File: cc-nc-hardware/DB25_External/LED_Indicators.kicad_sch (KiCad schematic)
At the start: 6 parts, among them U8 74HC14

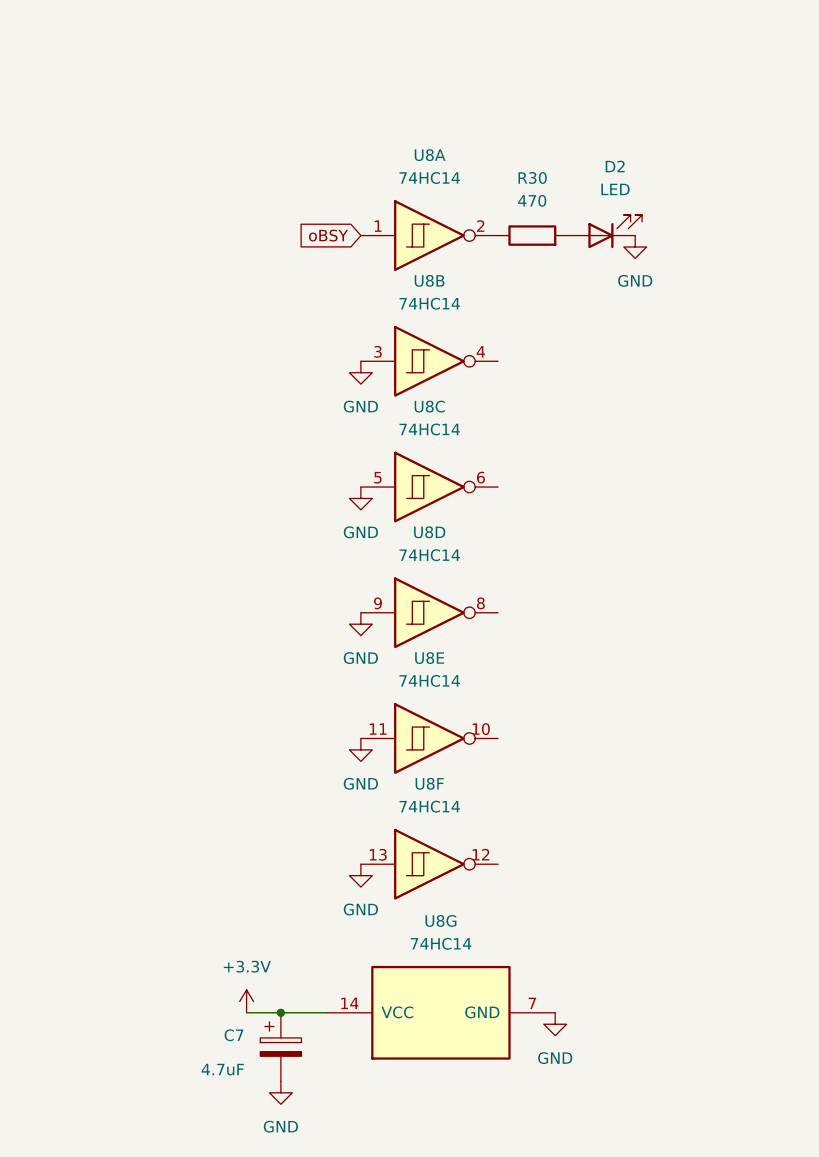
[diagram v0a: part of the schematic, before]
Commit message: DB25 2023_06a, Smaller Design
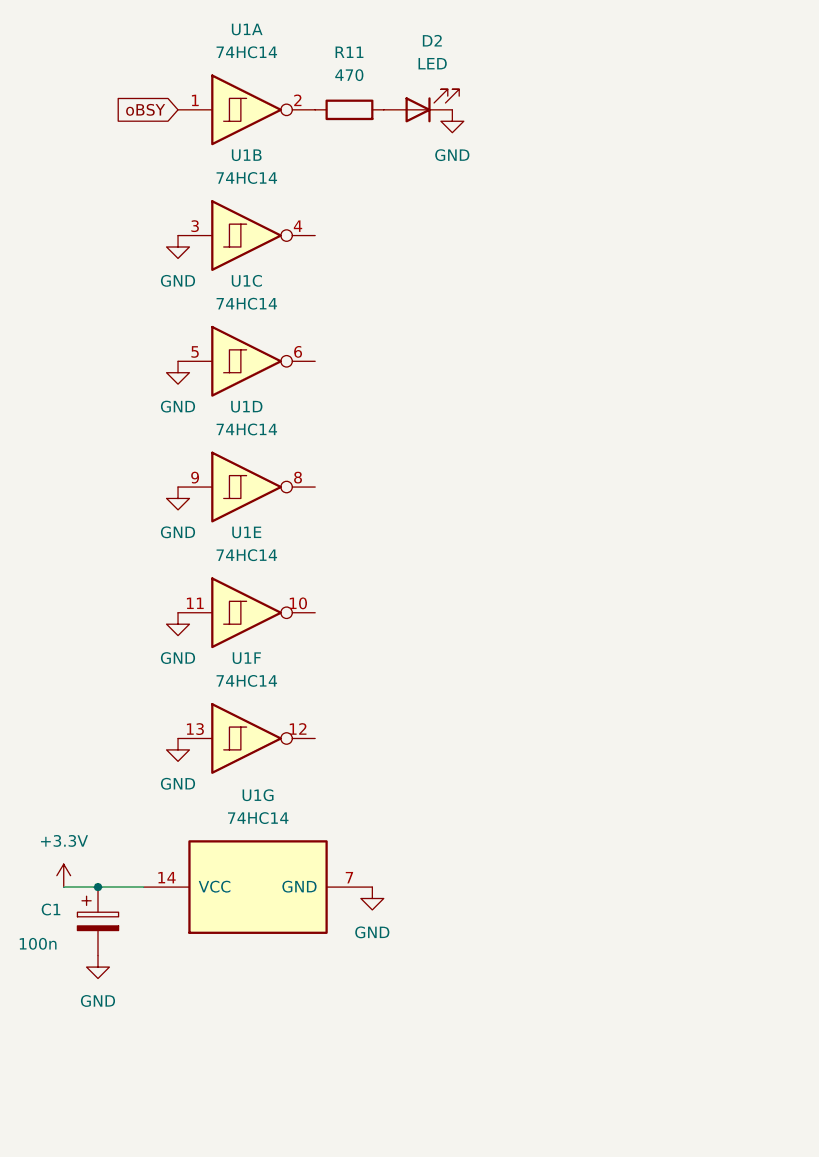
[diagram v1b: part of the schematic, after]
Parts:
- removed C7: 4.7uF, Capacitor_SMD:C_0805_2012Metric_Pad1.18x1.45mm_HandSolder, symbol Device:CP
- removed R30: 470, Resistor_SMD:R_0402_1005Metric_Pad0.72x0.64mm_HandSolder, symbol Device:R
- removed U8: 74HC14, symbol 74xx:74HC14
- added C1: 100n, Capacitor_SMD:C_0805_2012Metric_Pad1.18x1.45mm_HandSolder, symbol Device:CP
- added R11: 470, Resistor_SMD:R_0603_1608Metric_Pad0.98x0.95mm_HandSolder, symbol Device:R
- added U1: 74HC14, symbol 74xx:74HC14
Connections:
- net +3V3: now also C1.1, U1.14 (VCC)
- net GND: now also C1.2, U1.11, U1.13, U1.3, U1.5, U1.7 (GND), U1.9
- net oBSY: now also U1.1
- net at D2.2 (A): now also R11.2
- new net: R11.1, U1.2

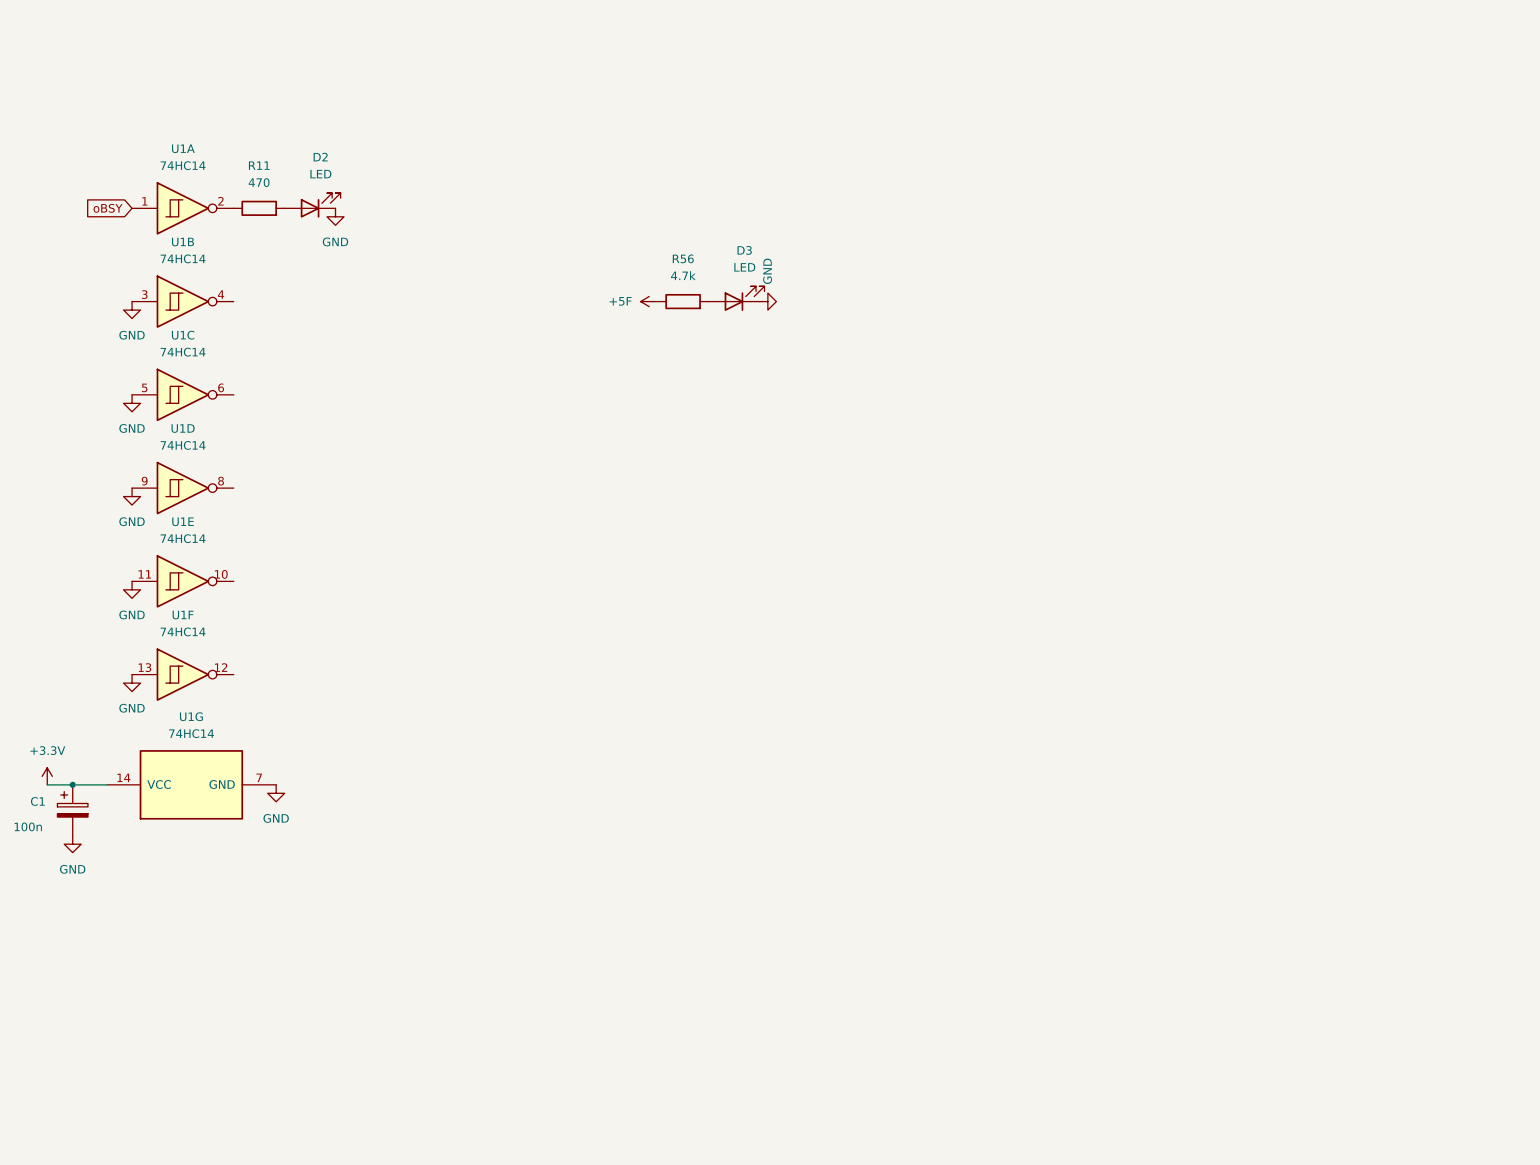
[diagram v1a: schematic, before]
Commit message: Update DB25 schematic for greater clarity
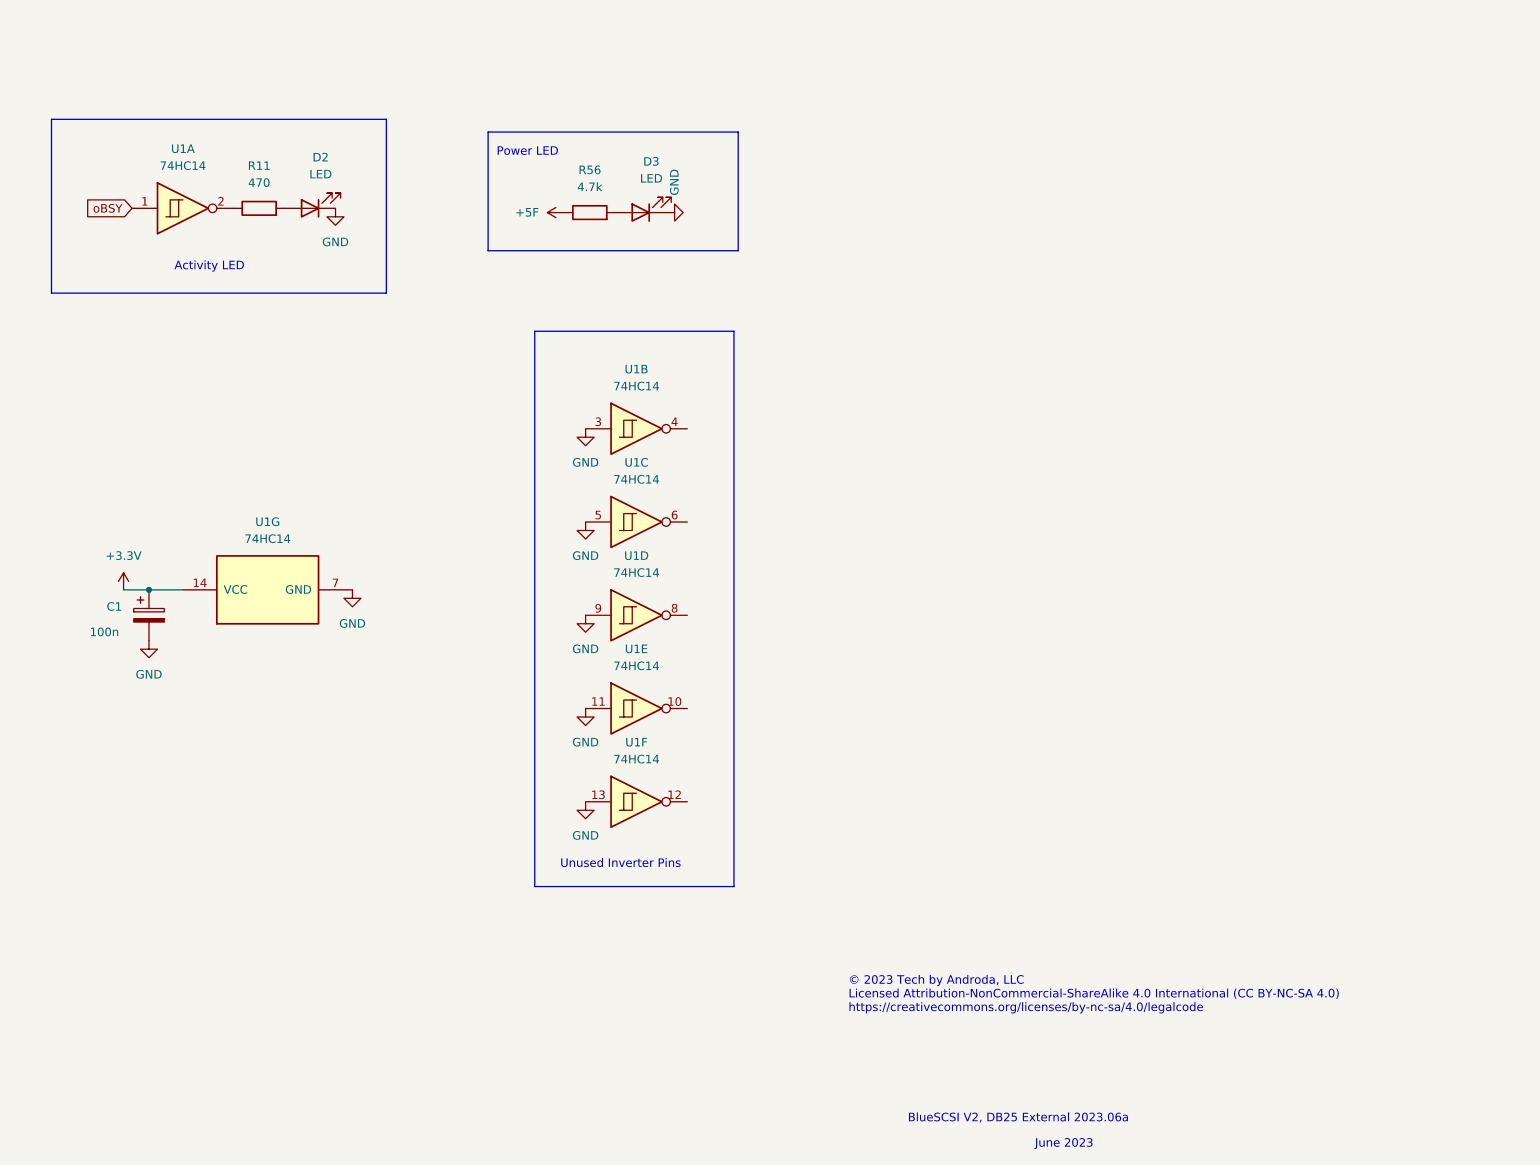
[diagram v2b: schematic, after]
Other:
- note added: "Activity LED"
- note added: "BlueSCSI V2, DB25 External 2023.06a"
- note added: "June 2023"
- note added: "Power LED"
- note added: "Unused Inverter Pins"
- note added: "© 2023 Tech by Androda, LLC Licensed Attribution-NonCommercial-ShareAlike 4.0 International (CC BY-NC-SA 4.0) https://creativecommons.org/licenses/by-nc-sa/4.0/legalcode"
- moved on the sheet: C1, D3, R56, U1B, U1C, U1D, U1E, U1F, U1G

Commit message: DB25 Hardware Version 2024.01a, Narrower
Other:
- note added: "BlueSCSI V2, DB25 External 2024.01a"
- note added: "January 2024"
- note added: "© 2023 - 2024 Tech by Androda, LLC Licensed Attribution-NonCommercial-ShareAlike 4.0 International (CC BY-NC-SA 4.0) https://creativecommons.org/licenses/by-nc-sa/4.0/legalcode"
- note removed: "BlueSCSI V2, DB25 External 2023.06a"
- note removed: "June 2023"
- note removed: "© 2023 Tech by Androda, LLC Licensed Attribution-NonCommercial-ShareAlike 4.0 International (CC BY-NC-SA 4.0) https://creativecommons.org/licenses/by-nc-sa/4.0/legalcode"
- moved on the sheet: C1, D2, D3, R11, R56, U1A, U1B, U1C, U1D, U1E, U1F, U1G
